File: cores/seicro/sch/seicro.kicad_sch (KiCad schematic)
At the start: 0 parts

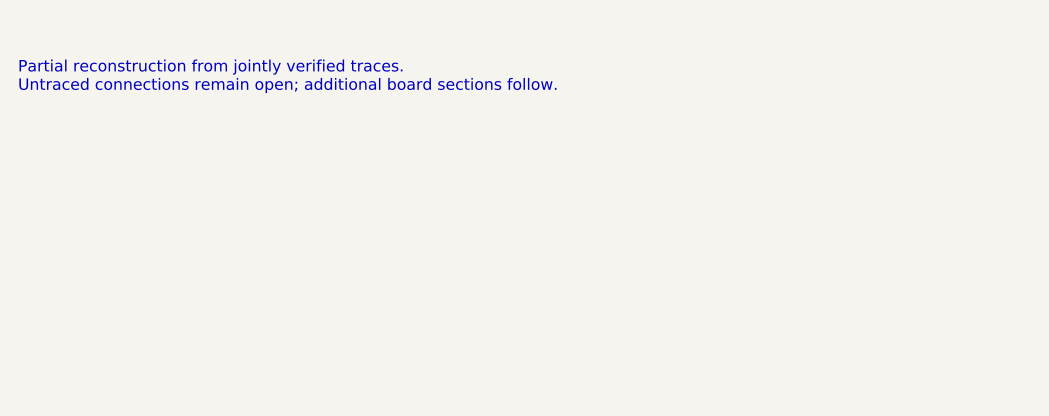
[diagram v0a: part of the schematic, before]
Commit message: feat(seicro): add CD RAM schematic sheet
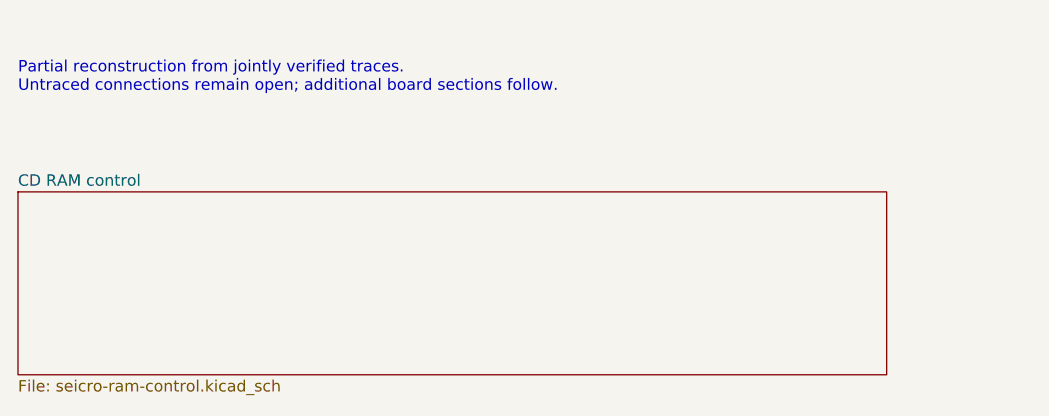
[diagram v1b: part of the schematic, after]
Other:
- added sheet CD RAM control (seicro-ram-control.kicad_sch)
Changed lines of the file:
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@@
 (text "Priority, palette selection, latch\nand PROM bank/address enables" (at 153.67 149.86 0) (effects (font (size 1.27 1.27)) (justify left)))
 (text "Partial reconstruction from jointly verified traces.\nUntraced connections remain open; additional board sections follow." (at 25.4 172.72 0) (effects (font (size 1.27 1.27)) (justify left)))
+(sheet (at 25.4 185.42) (size 96.52 20.32) (fields_autoplaced) (stroke (width 0) (type default)) (fill (color 0 0 0 0)) (property "Sheetname" "CD RAM control" (at 25.4 184.15 0) (effects (font (size 1.27 1.27)) (justify left))) (property "Sheetfile" "seicro-ram-control.kicad_sch" (at 25.4 207.01 0) (effects (font (size 1.27 1.27)) (justify left))) (instances (project "seicro" (path "/c2fd9126-7b79-5cad-8364-4b1ad0db9811" (page "5")))))
 (sheet_instances (path "/" (page "1")))
 )

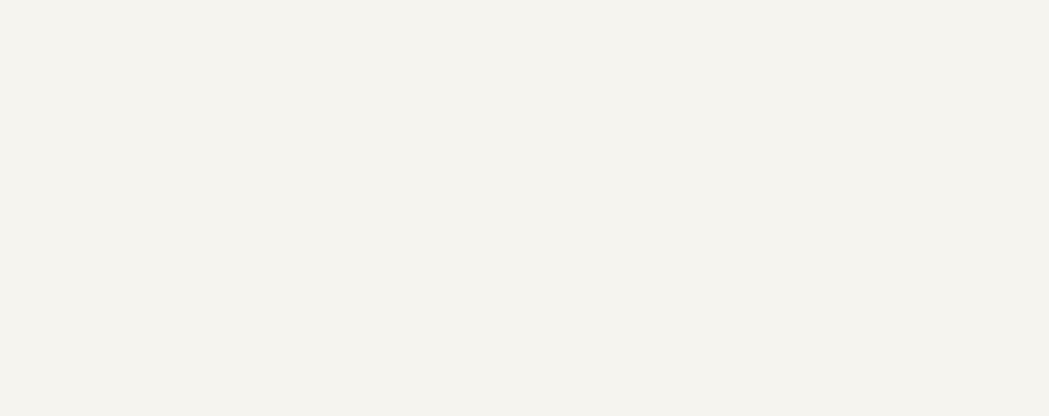
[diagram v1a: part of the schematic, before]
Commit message: feat(seicro): add CD address counter sheet
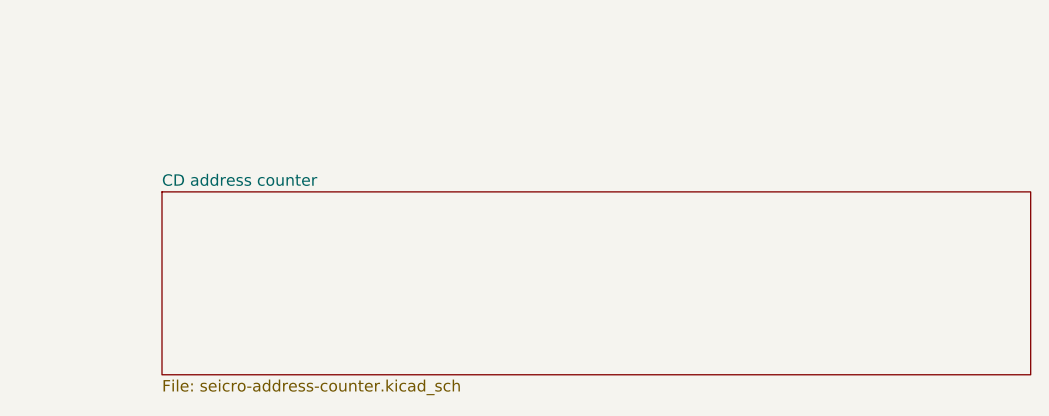
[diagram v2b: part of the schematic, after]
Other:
- added sheet CD address counter (seicro-address-counter.kicad_sch)
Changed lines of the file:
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@@
 (text "Partial reconstruction from jointly verified traces.\nUntraced connections remain open; additional board sections follow." (at 25.4 172.72 0) (effects (font (size 1.27 1.27)) (justify left)))
 (sheet (at 25.4 185.42) (size 96.52 20.32) (fields_autoplaced) (stroke (width 0) (type default)) (fill (color 0 0 0 0)) (property "Sheetname" "CD RAM control" (at 25.4 184.15 0) (effects (font (size 1.27 1.27)) (justify left))) (property "Sheetfile" "seicro-ram-control.kicad_sch" (at 25.4 207.01 0) (effects (font (size 1.27 1.27)) (justify left))) (instances (project "seicro" (path "/c2fd9126-7b79-5cad-8364-4b1ad0db9811" (page "5")))))
+(sheet (at 153.67 185.42) (size 96.52 20.32) (fields_autoplaced) (stroke (width 0) (type default)) (fill (color 0 0 0 0)) (property "Sheetname" "CD address counter" (at 153.67 184.15 0) (effects (font (size 1.27 1.27)) (justify left))) (property "Sheetfile" "seicro-address-counter.kicad_sch" (at 153.67 207.01 0) (effects (font (size 1.27 1.27)) (justify left))) (instances (project "seicro" (path "/c2fd9126-7b79-5cad-8364-4b1ad0db9811" (page "6")))))
 (sheet_instances (path "/" (page "1")))
 )

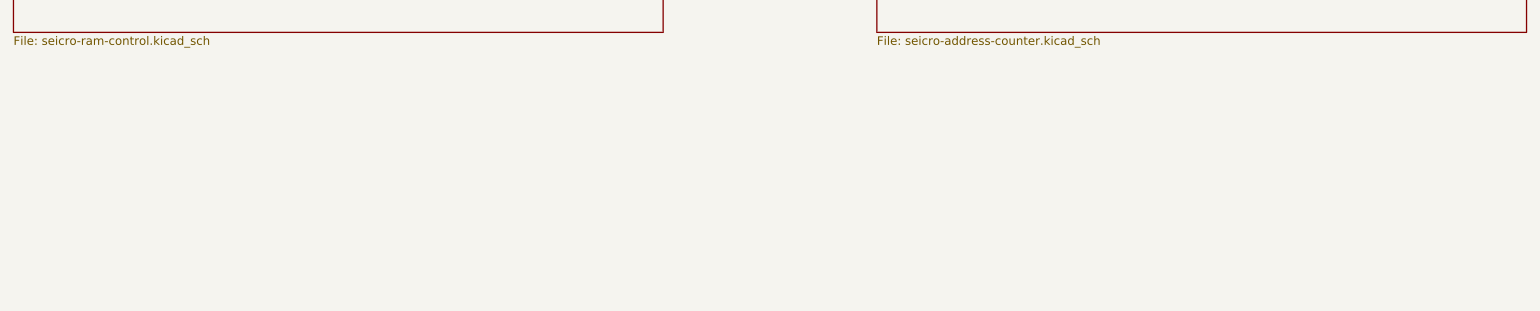
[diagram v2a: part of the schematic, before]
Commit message: feat(seicro): add chip placement sheets
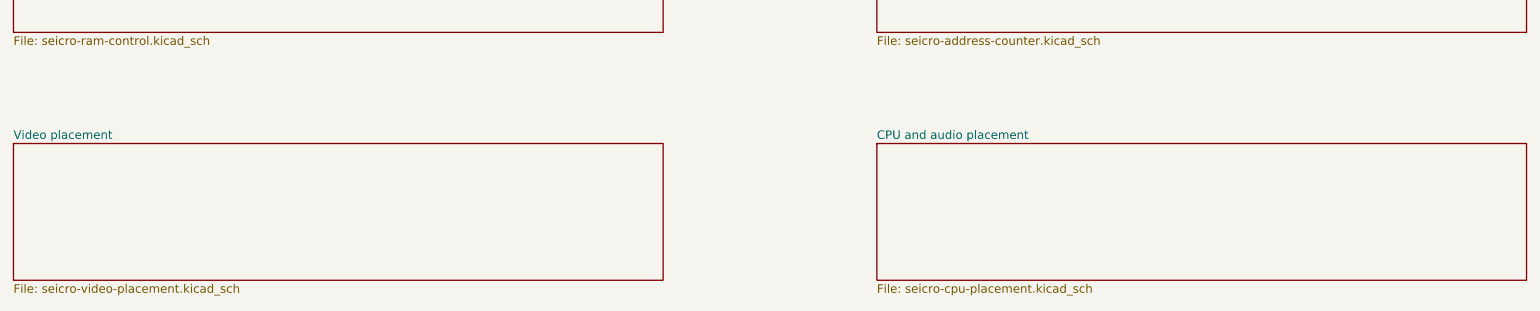
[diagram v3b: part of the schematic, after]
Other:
- added sheet CPU and audio placement (seicro-cpu-placement.kicad_sch)
- added sheet Video placement (seicro-video-placement.kicad_sch)
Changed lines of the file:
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@@
 (sheet (at 25.4 185.42) (size 96.52 20.32) (fields_autoplaced) (stroke (width 0) (type default)) (fill (color 0 0 0 0)) (property "Sheetname" "CD RAM control" (at 25.4 184.15 0) (effects (font (size 1.27 1.27)) (justify left))) (property "Sheetfile" "seicro-ram-control.kicad_sch" (at 25.4 207.01 0) (effects (font (size 1.27 1.27)) (justify left))) (instances (project "seicro" (path "/c2fd9126-7b79-5cad-8364-4b1ad0db9811" (page "5")))))
 (sheet (at 153.67 185.42) (size 96.52 20.32) (fields_autoplaced) (stroke (width 0) (type default)) (fill (color 0 0 0 0)) (property "Sheetname" "CD address counter" (at 153.67 184.15 0) (effects (font (size 1.27 1.27)) (justify left))) (property "Sheetfile" "seicro-address-counter.kicad_sch" (at 153.67 207.01 0) (effects (font (size 1.27 1.27)) (justify left))) (instances (project "seicro" (path "/c2fd9126-7b79-5cad-8364-4b1ad0db9811" (page "6")))))
+(sheet (at 25.4 222.25) (size 96.52 20.32) (fields_autoplaced) (stroke (width 0) (type default)) (fill (color 0 0 0 0)) (property "Sheetname" "Video placement" (at 25.4 220.98 0) (effects (font (size 1.27 1.27)) (justify left))) (property "Sheetfile" "seicro-video-placement.kicad_sch" (at 25.4 243.84 0) (effects (font (size 1.27 1.27)) (justify left))) (instances (project "seicro" (path "/c2fd9126-7b79-5cad-8364-4b1ad0db9811" (page "7")))))
+(sheet (at 153.67 222.25) (size 96.52 20.32) (fields_autoplaced) (stroke (width 0) (type default)) (fill (color 0 0 0 0)) (property "Sheetname" "CPU and audio placement" (at 153.67 220.98 0) (effects (font (size 1.27 1.27)) (justify left))) (property "Sheetfile" "seicro-cpu-placement.kicad_sch" (at 153.67 243.84 0) (effects (font (size 1.27 1.27)) (justify left))) (instances (project "seicro" (path "/c2fd9126-7b79-5cad-8364-4b1ad0db9811" (page "8")))))
 (sheet_instances (path "/" (page "1")))
 )
